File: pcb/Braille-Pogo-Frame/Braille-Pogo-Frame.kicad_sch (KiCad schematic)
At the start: 24 parts, among them J101 Conn_01x06, J102 Conn_01x06, J103 Conn_01x06, J104 Conn_01x06, J105 Conn_01x06, J106 Conn_01x06, J107 Conn_01x06, J108 Conn_01x06

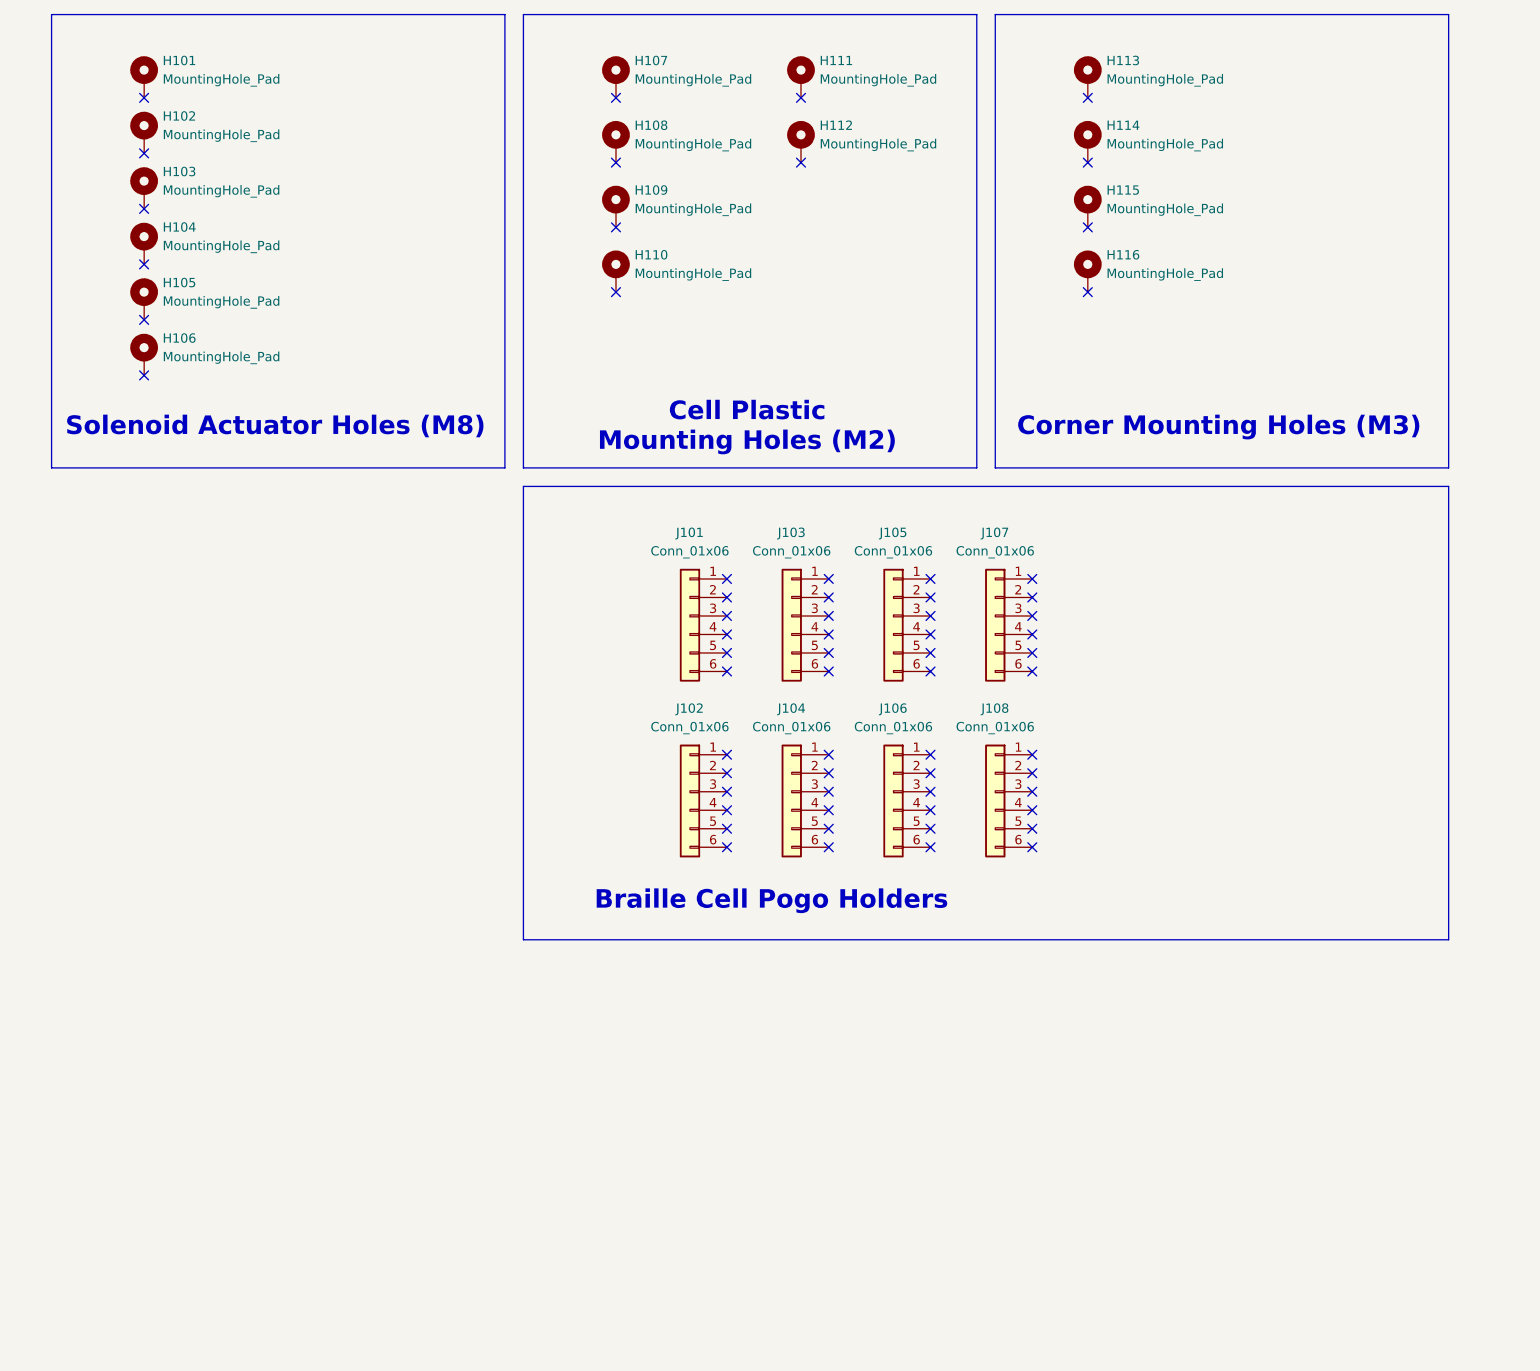
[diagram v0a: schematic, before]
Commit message: Refactor Braille Cells, add Stepper footprint
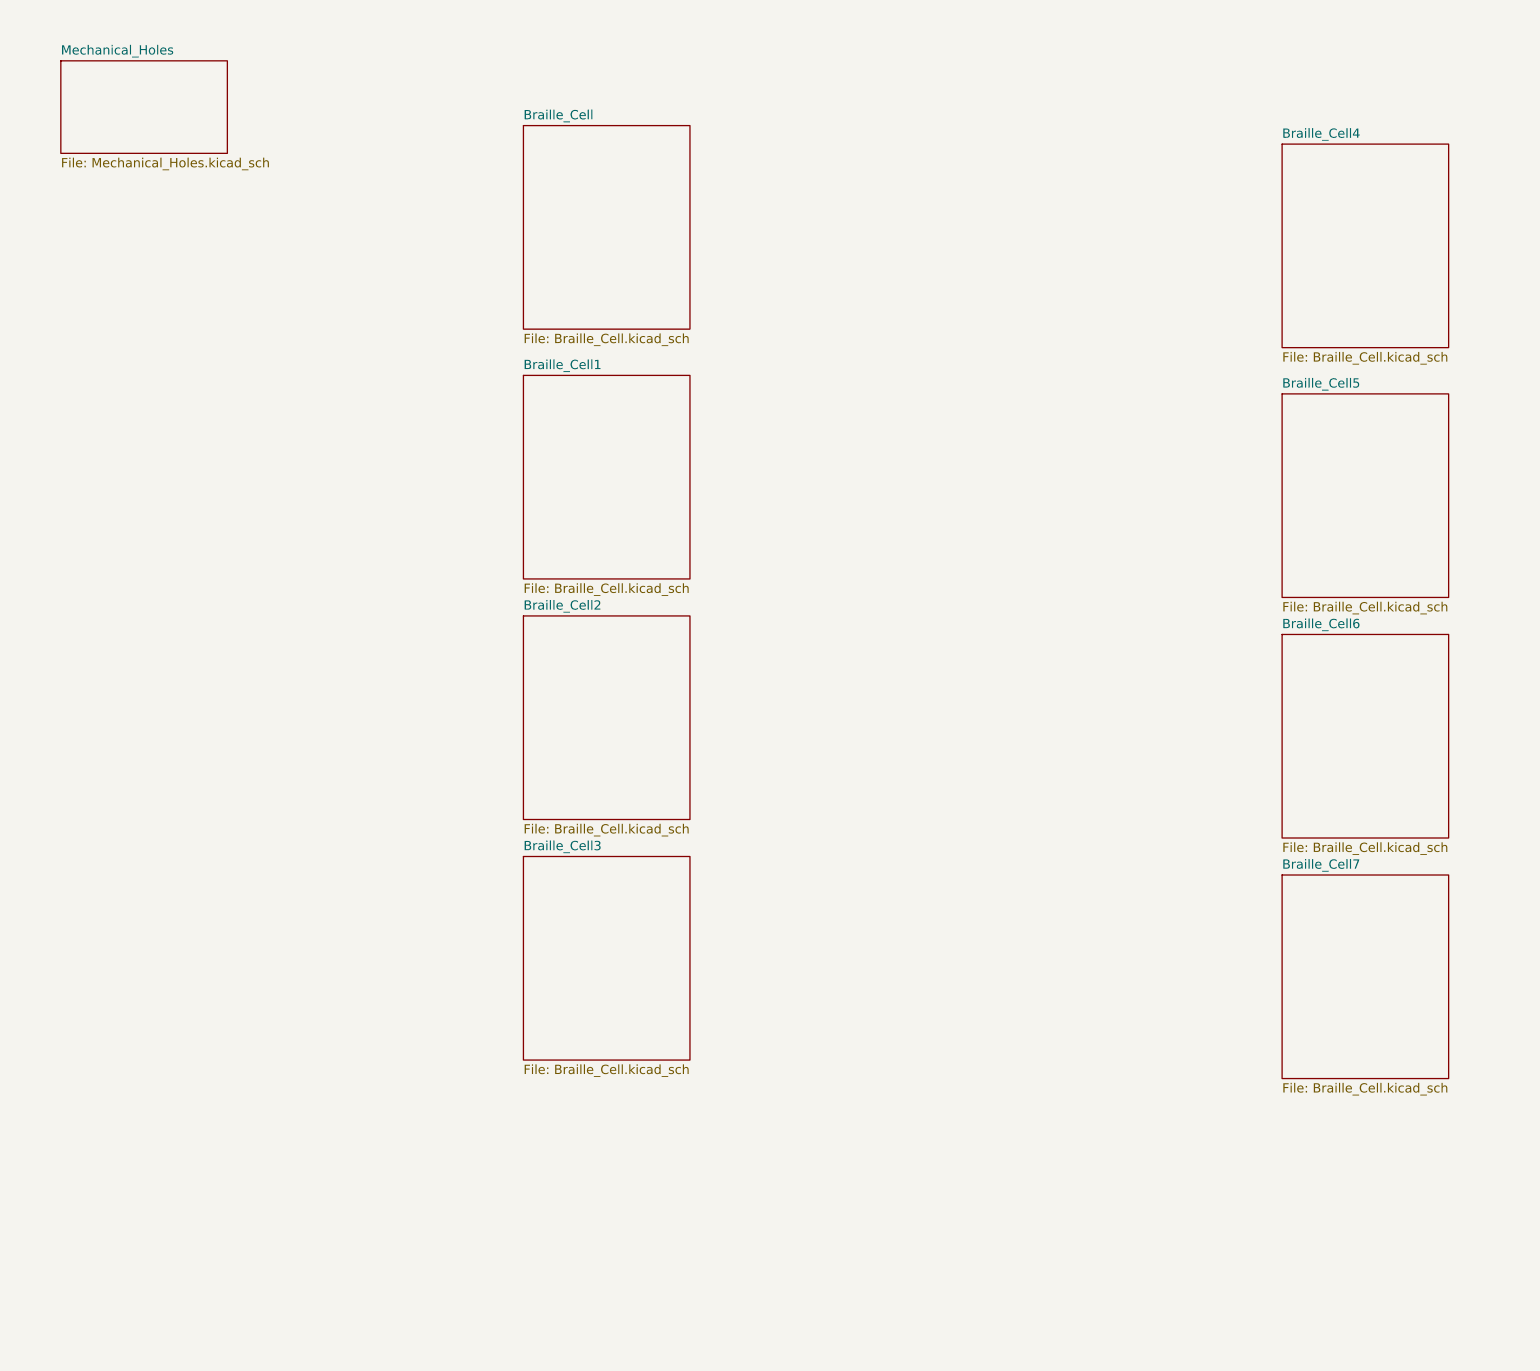
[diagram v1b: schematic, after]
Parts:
- removed H101, H102, H103, H104, H105, H106: MountingHole_Pad, 00-lib-footprints:MountingHole_8mm_Rect_NoSilk, symbol Mechanical:MountingHole_Pad
- removed H107, H108, H109, H110, H111, H112: MountingHole_Pad, 00-lib-footprints:MountingHole_2.2mm_M2_Pad_NoSilk, symbol Mechanical:MountingHole_Pad
- removed H113, H114, H115, H116: MountingHole_Pad, 00-lib-footprints:MountingHole_3.2mm_M3_Pad_NoSilk, symbol Mechanical:MountingHole_Pad
- removed J101, J102, J103, J104, J105, J106, J107, J108: Conn_01x06, 00-lib-footprints:Braille_Cell_Pogos_Solder_2.5mmIntra_6.6x10mmInter, symbol Connector_Generic:Conn_01x06
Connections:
- no-connect marks 64 -> 0
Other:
- added sheet Braille_Cell (Braille_Cell.kicad_sch)
- added sheet Braille_Cell1 (Braille_Cell.kicad_sch)
- added sheet Braille_Cell2 (Braille_Cell.kicad_sch)
- added sheet Braille_Cell3 (Braille_Cell.kicad_sch)
- added sheet Braille_Cell4 (Braille_Cell.kicad_sch)
- added sheet Braille_Cell5 (Braille_Cell.kicad_sch)
- added sheet Braille_Cell6 (Braille_Cell.kicad_sch)
- added sheet Braille_Cell7 (Braille_Cell.kicad_sch)
- added sheet Mechanical_Holes (Mechanical_Holes.kicad_sch)
- note removed: "Braille Cell Pogo Holders"
- note removed: "Cell Plastic Mounting Holes (M2)"
- note removed: "Corner Mounting Holes (M3)"
- note removed: "Solenoid Actuator Holes (M8)"

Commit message: PCB: Add motors and motor driver to schematic
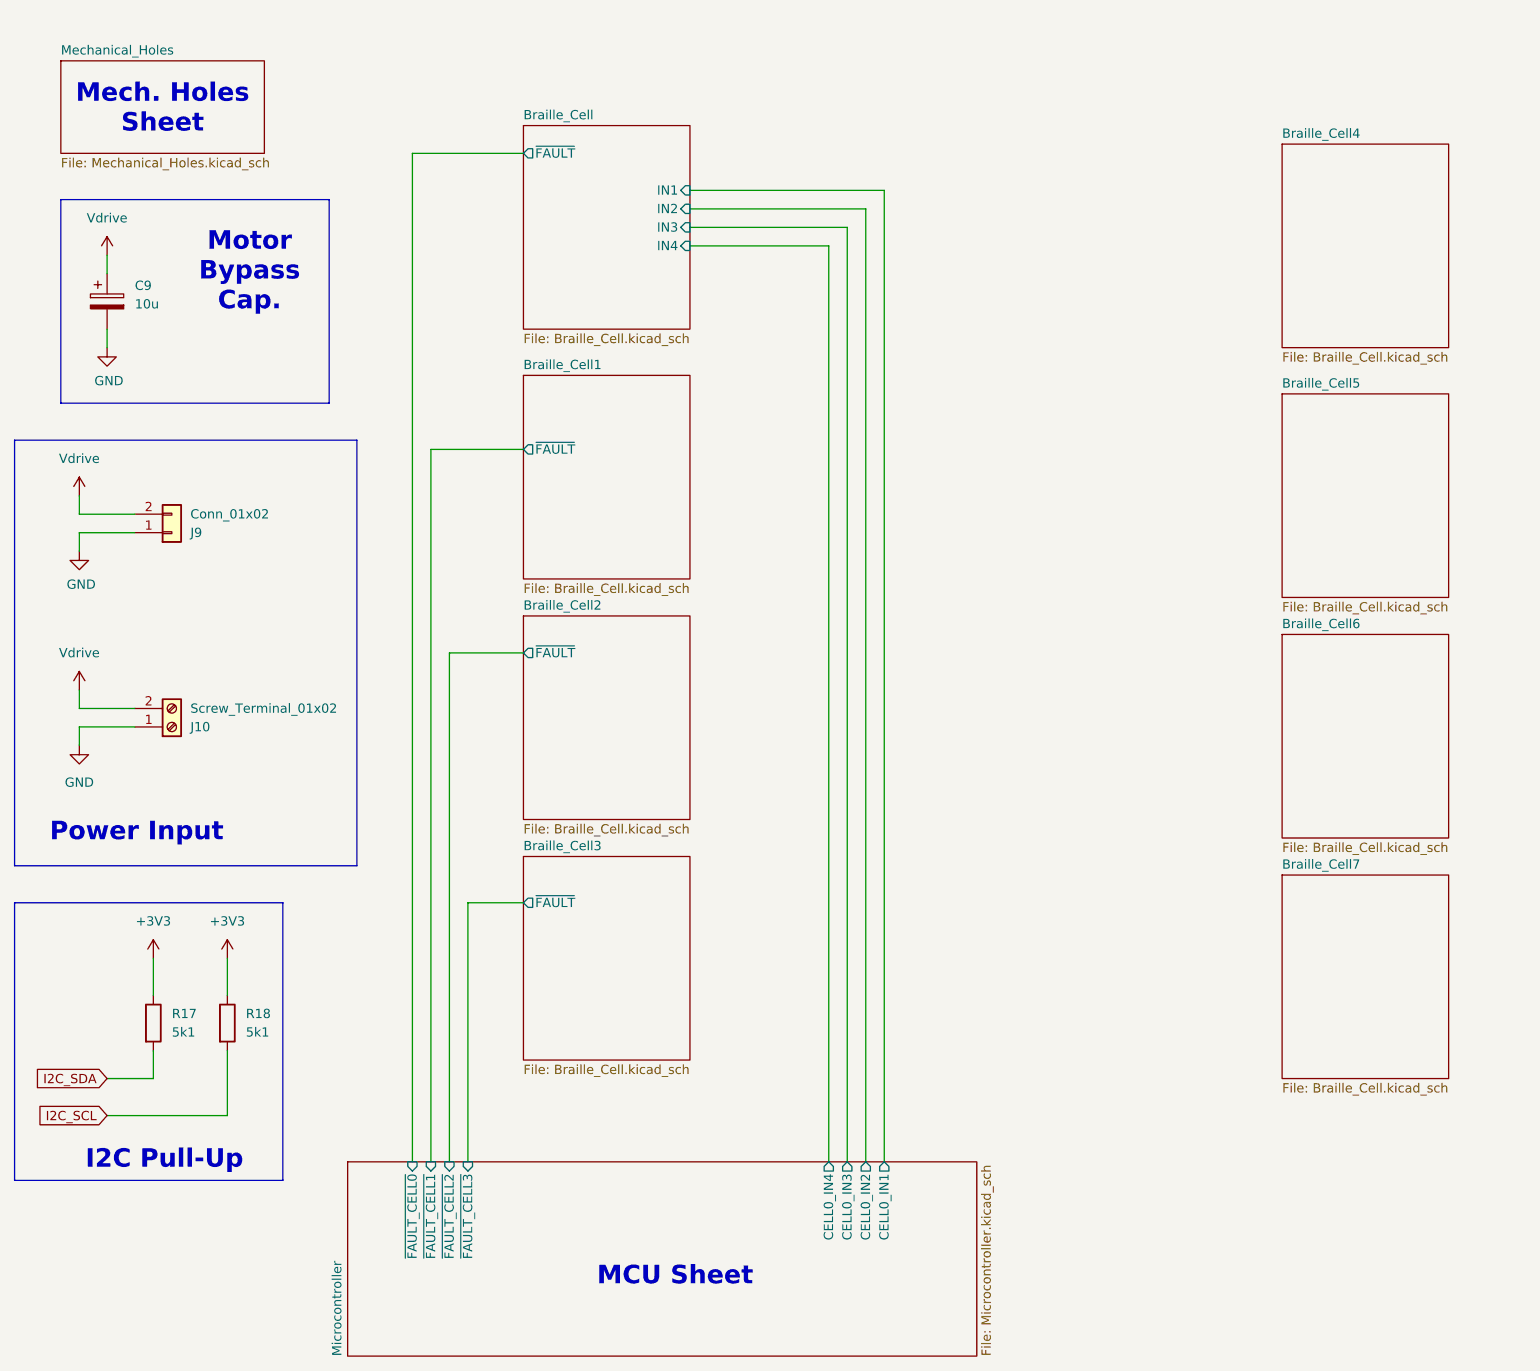
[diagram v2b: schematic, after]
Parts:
- added C9: 10u, symbol Device:C_Polarized
- added J10: Screw_Terminal_01x02, symbol Connector:Screw_Terminal_01x02
- added J9: Conn_01x02, symbol Connector_Generic:Conn_01x02
- added R17, R18: 5k1, symbol Device:R
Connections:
- new net +3V3: R17.1, R18.1
- new net GND: C9.2, J10.1 (Pin_1), J9.1 (Pin_1)
- new net I2C_SCL: R18.2
- new net I2C_SDA: R17.2
- new net Vdrive: C9.1, J10.2 (Pin_2), J9.2 (Pin_2)
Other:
- added sheet Microcontroller (Microcontroller.kicad_sch)
- sheet Braille_Cell ports: added IN1, IN2, IN3, IN4, ~{FAULT}; removed none
- sheet Braille_Cell1 ports: added ~{FAULT}; removed none
- sheet Braille_Cell2 ports: added ~{FAULT}; removed none
- sheet Braille_Cell3 ports: added ~{FAULT}; removed none
- note added: "I2C Pull-Up"
- note added: "MCU Sheet"
- note added: "Mech. Holes Sheet"
- note added: "Motor Bypass Cap."
- note added: "Power Input"

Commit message: PCB: Update footprint assignments
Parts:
- C9: footprint (none) -> Capacitor_THT:CP_Radial_D6.3mm_P2.50mm
- J10: footprint (none) -> TerminalBlock:TerminalBlock_bornier-2_P5.08mm
- J9: footprint (none) -> Connector_PinHeader_2.54mm:PinHeader_1x02_P2.54mm_Vertical
- R17, R18: footprint (none) -> Resistor_SMD:R_1206_3216Metric_Pad1.30x1.75mm_HandSolder
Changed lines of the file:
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@@
 			)
 		)
-		(property "Footprint" ""
+		(property "Footprint" "TerminalBlock:TerminalBlock_bornier-2_P5.08mm"
 			(at 41.91 113.03 0)
 			(effects
@@
 			)
 		)
-		(property "Footprint" ""
+		(property "Footprint" "Connector_PinHeader_2.54mm:PinHeader_1x02_P2.54mm_Vertical"
 			(at 41.91 86.36 0)
 			(effects
@@
 			)
 		)
-		(property "Footprint" ""
+		(property "Footprint" "Resistor_SMD:R_1206_3216Metric_Pad1.30x1.75mm_HandSolder"
 			(at 47.752 153.67 90)
 			(effects
@@
 			)
 		)
-		(property "Footprint" ""
+		(property "Footprint" "Capacitor_THT:CP_Radial_D6.3mm_P2.50mm"
 			(at 33.9852 58.42 0)
 			(effects
@@
 			)
 		)
-		(property "Footprint" ""
+		(property "Footprint" "Resistor_SMD:R_1206_3216Metric_Pad1.30x1.75mm_HandSolder"
 			(at 37.592 153.67 90)
 			(effects
